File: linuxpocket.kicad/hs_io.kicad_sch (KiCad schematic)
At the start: 3 parts, among them J3 HDMI_C_1.4

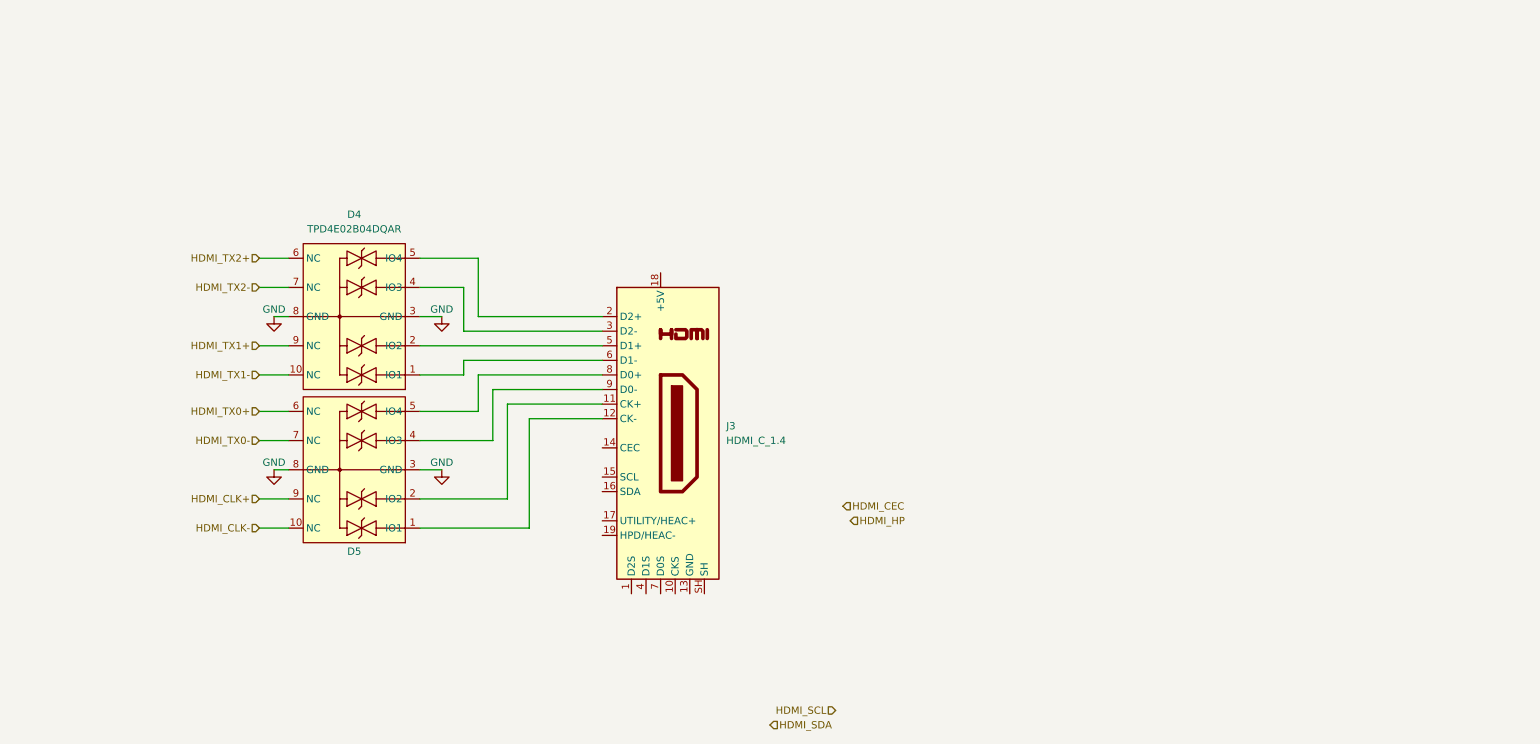
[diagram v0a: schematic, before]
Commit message: Finish HDMI
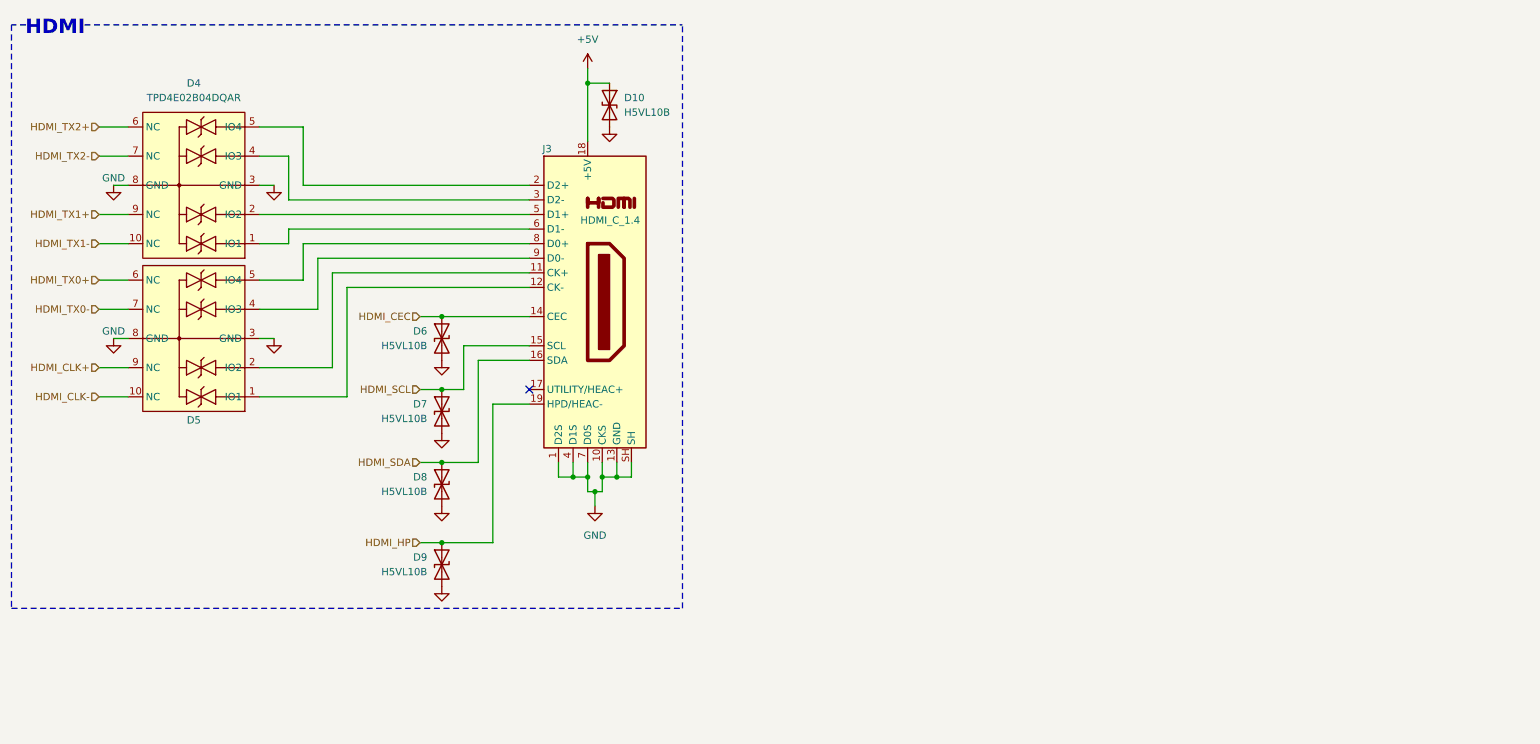
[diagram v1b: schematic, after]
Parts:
- added D10, D6, D7, D8, D9: H5VL10B, Diode_SMD:D_SOD-882, symbol Device:D_TVS
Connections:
- net GND: now also J3.1 (D2S), J3.10 (CKS), J3.13 (GND), J3.4 (D1S), J3.7 (D0S), J3.SH, D10.2 (A2), D6.2 (A2), D7.2 (A2), D8.2 (A2), D9.2 (A2)
- net HDMI_CEC: now also J3.14 (CEC), D6.1 (A1)
- net HDMI_HP: now also J3.19 (HPD/HEAC-), D9.1 (A1)
- net HDMI_SCL: now also J3.15 (SCL), D7.1 (A1)
- net HDMI_SDA: now also J3.16 (SDA), D8.1 (A1)
- net +5V: now reaches J3.18 (+5V)
- net +5V: now also D10.1 (A1)
- no-connect marks 0 -> 1
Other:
- note added: "HDMI"
- moved on the sheet: D4, D5, J3

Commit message: Finish USB-C. #1
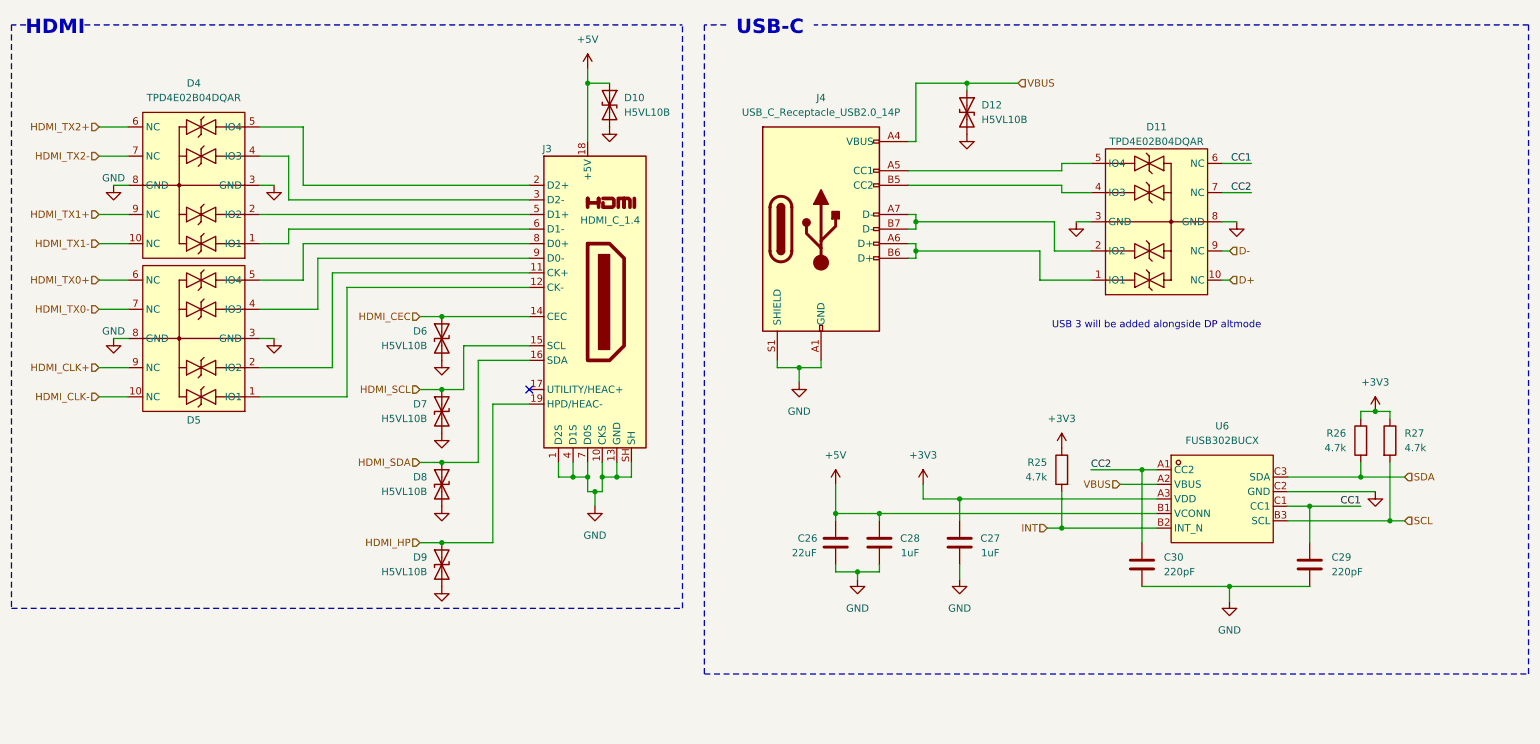
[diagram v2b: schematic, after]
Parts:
- added C26: 22uF, symbol Device:C
- added C27, C28: 1uF, Capacitor_SMD:C_0402_1005Metric, symbol Device:C
- added C29, C30: 220pF, Capacitor_SMD:C_0402_1005Metric, symbol Device:C
- added D11: TPD4E02B04DQAR, linuxpocket:USON-10_L2.5-W1.0-P0.50-BL, symbol linuxpocket:TPD4E02B04DQAR
- added D12: H5VL10B, Diode_SMD:D_SOD-882, symbol Device:D_TVS
- added J4: USB_C_Receptacle_USB2.0_14P, symbol Connector:USB_C_Receptacle_USB2.0_14P
- added R25, R26, R27: 4.7k, Resistor_SMD:R_0402_1005Metric, symbol Device:R
- added U6: FUSB302BUCX, linuxpocket:WLCSP-9_L1.3-W1.2-R3-C3-P0.40-TL, symbol linuxpocket:FUSB302BUCX
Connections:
- net +5V: now also C26.1, C28.2, U6.B1 (VCONN)
- net GND: now also C26.2, C27.1, C28.1, C29.2, C30.2, D11.3 (GND), D11.8 (GND), D12.2 (A2), J4.A1 (GND), J4.A12 (GND), J4.B1 (GND), J4.B12 (GND), J4.S1 (SHIELD), U6.C2 (GND)
- new net: D11.1 (IO1), J4.A6 (D+), J4.B6 (D+)
- new net: D11.2 (IO2), J4.A7 (D-), J4.B7 (D-)
- new net: D11.4 (IO3), J4.B5 (CC2)
- new net: D11.5 (IO4), J4.A5 (CC1)
- new net +3V3: C27.2, R25.1, R26.1, R27.1, U6.A3 (VDD)
- new net CC1: C29.1, D11.6 (NC), U6.C1 (CC1)
- new net CC2: C30.1, D11.7 (NC), U6.A1 (CC2)
- new net D+: D11.10 (NC)
- new net D-: D11.9 (NC)
- new net INT: R25.2, U6.B2 (INT_N)
- new net SCL: R27.2, U6.B3 (SCL)
- new net SDA: R26.2, U6.C3 (SDA)
- new net VBUS: D12.1 (A1), J4.A4 (VBUS), J4.A9 (VBUS), J4.B4 (VBUS), J4.B9 (VBUS), U6.A2 (VBUS)
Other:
- note added: "USB 3 will be added alongside DP altmode"
- note added: "USB-C"

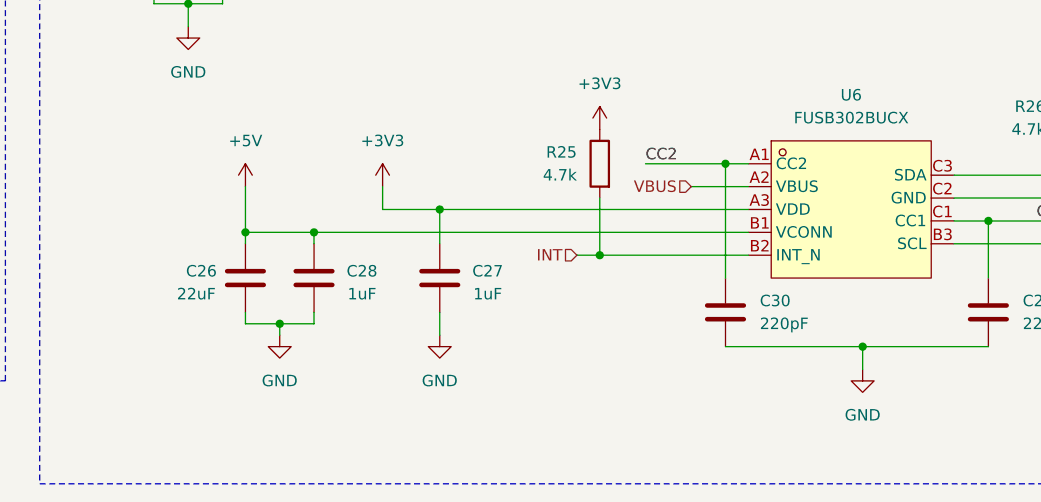
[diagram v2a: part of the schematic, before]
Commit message: Add magnetometer #5. Add footprints to some symbols.
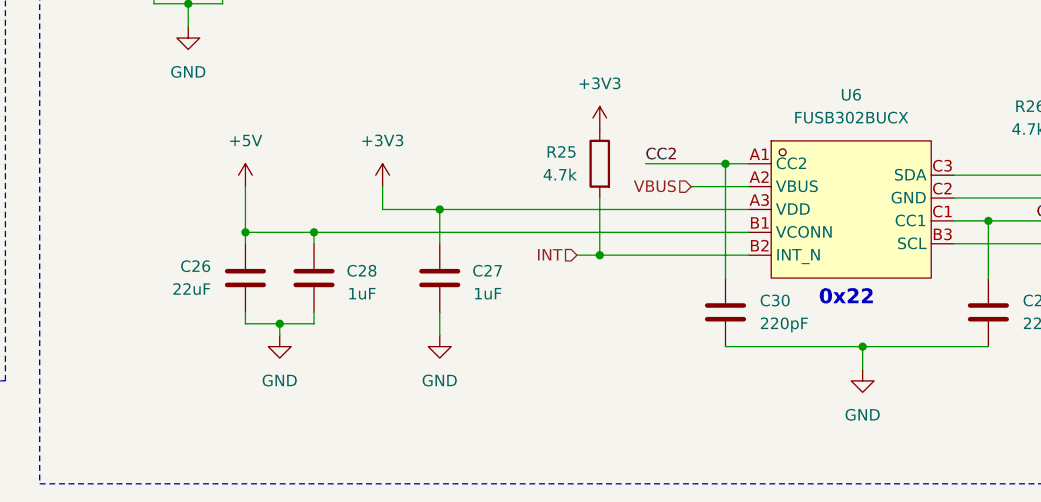
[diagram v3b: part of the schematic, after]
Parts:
- C26: footprint (none) -> Capacitor_SMD:C_0603_1608Metric; LCSC (none) -> C59461
- J3: footprint (none) -> linuxpocket:HDMI-SMD_A71-05H4-111N1; LCSC (none) -> C2682170
- J4: footprint (none) -> linuxpocket:USB-SMD_TYPE-C16PIN-1; LCSC (none) -> C5150972
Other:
- note added: "0x22"
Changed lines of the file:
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@@
 		)
 	)
+	(text "0x22"
+		(exclude_from_sim no)
+		(at 226.822 108.966 0)
+		(effects
+			(font
+				(size 1.65 1.65)
+				(thickness 0.33)
+				(bold yes)
+				(color 132 0 132 1)
+			)
+		)
+	)
 	(text "USB 3 will be added alongside DP altmode"
 		(exclude_from_sim no)
@@
 	(symbol
 		(lib_id "Device:C")
+		(at 160.02 106.68 0)
+		(mirror y)
+		(unit 1)
+		(exclude_from_sim no)
+		(in_bom yes)
+		(on_board yes)
+		(dnp no)
+		(property "Reference" "C26"
+			(at 156.21 105.4099 0)
+			(effects
+				(font
+					(size 1.27 1.27)
+				)
+				(justify left)
+			)
+		)
+		(property "Value" "22uF"
+			(at 156.21 107.9499 0)
+			(effects
+				(font
+					(size 1.27 1.27)
+				)
+				(justify left)
+			)
+		)
+		(property "Footprint" "Capacitor_SMD:C_0603_1608Metric"
+			(at 159.0548 110.49 0)
+			(effects
+				(font
+					(size 1.27 1.27)
+				)
+				(hide yes)
+			)
+		)
+		(property "Datasheet" "~"
+			(at 160.02 106.68 0)
+			(effects
+				(font
+					(size 1.27 1.27)
+				)
+				(hide yes)
+			)
+		)
+		(property "Description" "Unpolarized capacitor"
+			(at 160.02 106.68 0)
+			(effects
+				(font
+					(size 1.27 1.27)
+				)
+				(hide yes)
+			)
+		)
+		(property "LCSC" "C59461"
+			(at 160.02 106.68 0)
+			(effects
+				(font
+					(size 1.27 1.27)
+				)
+				(hide yes)
+			)
+		)
+		(pin "1"
+		)
+		(pin "2"
+		)
+		(instances
+			(project "linuxpocket"
+				(path "/de3771bf-b13a-459d-a957-6ff90f7da387/748cdf11-7804-4e37-b79e-0f3d48b13d4c"
+					(reference "C26")
+					(unit 1)
+				)
+			)
+		)
+	)
+	(symbol
+		(lib_id "Device:C")
 		(at 167.64 106.68 180)
 		(unit 1)
@@
 	)
 	(symbol
-		(lib_id "Device:C")
-		(at 160.02 106.68 0)
-		(mirror y)
-		(unit 1)
-		(exclude_from_sim no)
-		(in_bom yes)
-		(on_board yes)
-		(dnp no)
-		(property "Reference" "C26"
-			(at 153.416 105.918 0)
-			(effects
-				(font
-					(size 1.27 1.27)
-				)
-				(justify right)
-			)
-		)
-		(property "Value" "22uF"
-			(at 152.4 108.458 0)
-			(effects
-				(font
-					(size 1.27 1.27)
-				)
-				(justify right)
-			)
-		)
-		(property "Footprint" ""
-			(at 159.0548 110.49 0)
-			(effects
-				(font
-					(size 1.27 1.27)
-				)
-				(hide yes)
-			)
-		)
-		(property "Datasheet" "~"
-			(at 160.02 106.68 0)
-			(effects
-				(font
-					(size 1.27 1.27)
-				)
-				(hide yes)
-			)
-		)
-		(property "Description" "Unpolarized capacitor"
-			(at 160.02 106.68 0)
-			(effects
-				(font
-					(size 1.27 1.27)
-				)
-				(hide yes)
-			)
-		)
-		(pin "1"
-		)
-		(pin "2"
-		)
-		(instances
-			(project "linuxpocket"
-				(path "/de3771bf-b13a-459d-a957-6ff90f7da387/748cdf11-7804-4e37-b79e-0f3d48b13d4c"
-					(reference "C26")
-					(unit 1)
-				)
-			)
-		)
-	)
-	(symbol
 		(lib_id "power:GND")
 		(at 62.23 44.45 0)
@@
 			)
 		)
-		(property "Footprint" ""
+		(property "Footprint" "linuxpocket:USB-SMD_TYPE-C16PIN-1"
 			(at 161.29 52.07 0)
 			(effects
@@
 			)
 		)
+		(property "LCSC" "C5150972"
+			(at 157.48 52.07 0)
+			(effects
+				(font
+					(size 1.27 1.27)
+				)
+				(hide yes)
+			)
+		)
 		(pin "B6"
 		)
@@
 			)
 		)
-		(property "Footprint" ""
+		(property "Footprint" "linuxpocket:HDMI-SMD_A71-05H4-111N1"
 			(at 117.475 64.77 0)
 			(effects
@@
 			(at 116.84 64.77 0)
 			(effects
+				(font
+					(size 1.27 1.27)
+				)
+				(hide yes)
+			)
+		)
+		(property "LCSC" "C2682170"
+			(at 116.84 64.77 0)
+			(effects

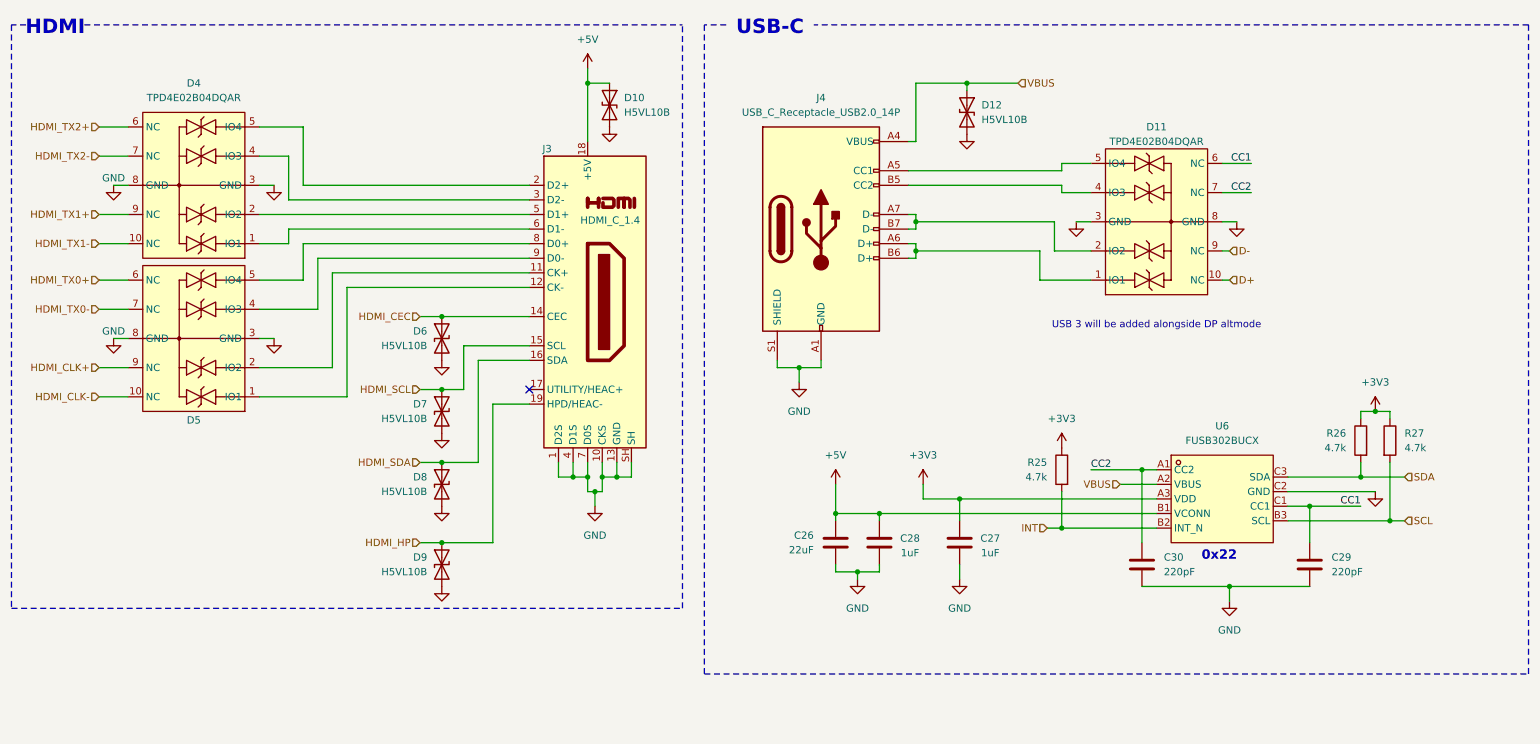
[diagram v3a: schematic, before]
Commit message: Start placing components in PCB.
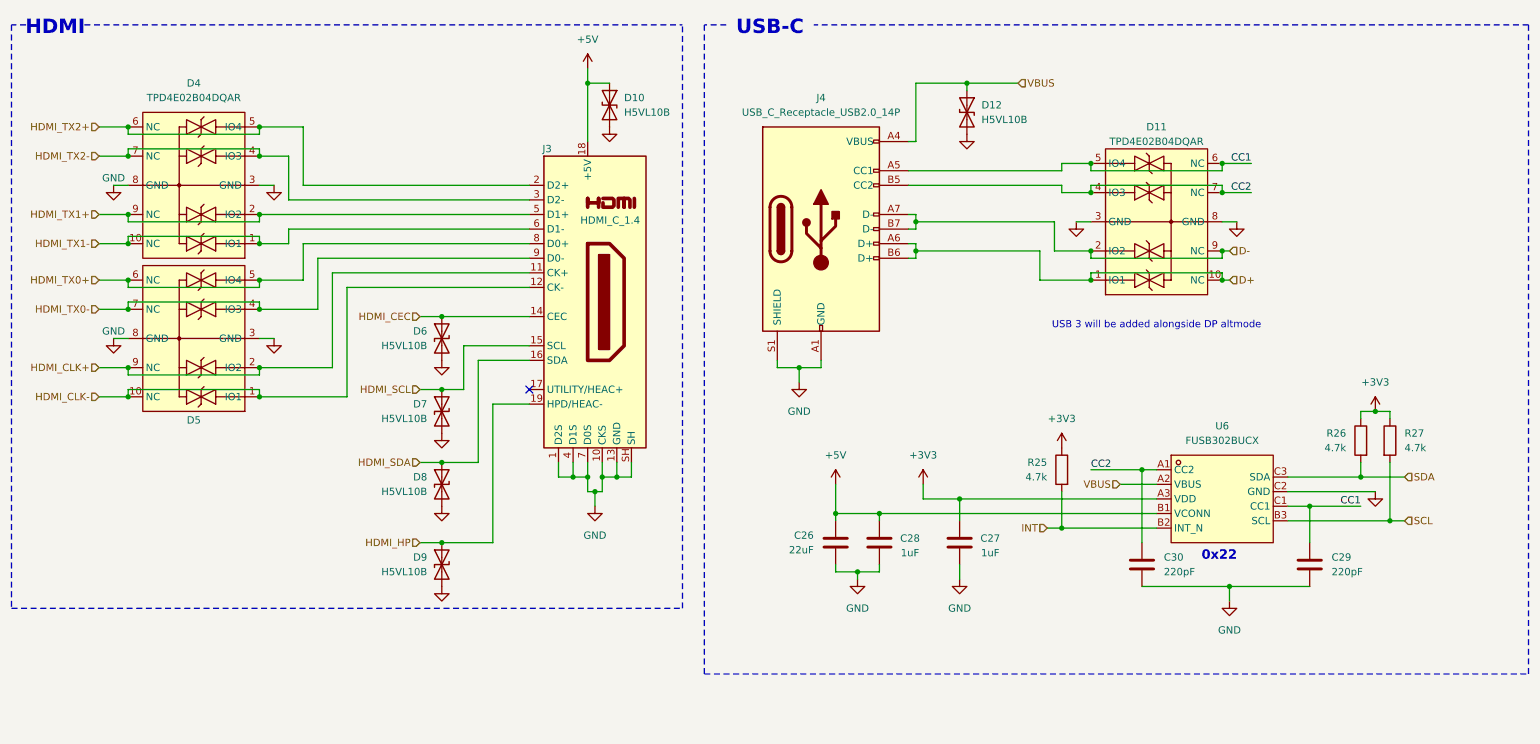
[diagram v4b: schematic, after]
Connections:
- net CC1: now also D11.5 (IO4), J4.A5 (CC1)
- net CC2: now also D11.4 (IO3), J4.B5 (CC2)
- net D+: now also D11.1 (IO1), J4.A6 (D+), J4.B6 (D+)
- net D-: now also D11.2 (IO2), J4.A7 (D-), J4.B7 (D-)
- net HDMI_CLK+: now also D5.2 (IO2), J3.11 (CK+)
- net HDMI_CLK-: now also D5.1 (IO1), J3.12 (CK-)
- net HDMI_TX0+: now also D5.5 (IO4), J3.8 (D0+)
- net HDMI_TX0-: now also D5.4 (IO3), J3.9 (D0-)
- net HDMI_TX1+: now also D4.2 (IO2), J3.5 (D1+)
- net HDMI_TX1-: now also D4.1 (IO1), J3.6 (D1-)
- net HDMI_TX2+: now also D4.5 (IO4), J3.2 (D2+)
- net HDMI_TX2-: now also D4.4 (IO3), J3.3 (D2-)

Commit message: PCB almost done and schematic finished.
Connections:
- net CC2: now also D11.1 (IO1), D11.10 (NC); no longer D11.4 (IO3), D11.7 (NC)
- net D+: now also D11.2 (IO2), D11.9 (NC); no longer D11.1 (IO1), D11.10 (NC)
- net D-: now also D11.4 (IO3), D11.7 (NC); no longer D11.2 (IO2), D11.9 (NC)
